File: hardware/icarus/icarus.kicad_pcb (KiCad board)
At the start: 2 copper layers, 0 parts

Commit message: Design with stm32f3
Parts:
- added C1: 1uF, Capacitor_SMD:C_0805_2012Metric, F.Cu at (167.6, 80.0)
- added C10: 10nF, Capacitor_SMD:C_0805_2012Metric, F.Cu at (182.6, 59.7)
- added C11: 100nF, Capacitor_SMD:C_0805_2012Metric, F.Cu at (182.6, 64.3)
- added C2: 1uF, Capacitor_SMD:C_0805_2012Metric, F.Cu at (160.3, 79.5)
- added C3: 4.7uF, Capacitor_SMD:C_0805_2012Metric, F.Cu at (158.0, 58.9)
- added C4: 100nF, Capacitor_SMD:C_0805_2012Metric, F.Cu at (183.9, 77.2)
- added C5: 100nF, Capacitor_SMD:C_0805_2012Metric, F.Cu at (158.0, 68.3)
- added C6: 100nF, Capacitor_SMD:C_0805_2012Metric, F.Cu at (162.1, 57.1)
- added C7: 100nF, Capacitor_SMD:C_0805_2012Metric, F.Cu at (169.2, 68.3)
- added C8: 100nF, Capacitor_SMD:C_0805_2012Metric, F.Cu at (182.6, 62.0)
- added C9: 2.2nF, Capacitor_SMD:C_0805_2012Metric, F.Cu at (174.0, 60.2)
- added D1: PWR, LED_SMD:LED_0805_2012Metric, F.Cu at (164.3, 75.4)
- added D2: STAT1, LED_SMD:LED_0805_2012Metric, F.Cu at (177.3, 54.4)
- added D3: STAT2, LED_SMD:LED_0805_2012Metric, F.Cu at (177.3, 56.6)
- added J1: USB_B_Micro, Connector_USB:USB_Micro-B_Amphenol_10103594-0001LF_Horizontal, F.Cu at (163.8, 86.4)
- added J2: SWJ-DP, Connector_PinHeader_1.27mm:PinHeader_2x05_P1.27mm_Vertical_SMD, F.Cu at (176.8, 71.4)
- added J3: PWR, Connector_PinSocket_2.54mm:PinSocket_1x06_P2.54mm_Vertical, F.Cu at (151.1, 54.6)
- added J4: PWM, Connector_PinSocket_2.54mm:PinSocket_1x06_P2.54mm_Vertical, F.Cu at (178.1, 49.5)
- added J5: COMMS, Connector_PinSocket_2.54mm:PinSocket_1x06_P2.54mm_Vertical, F.Cu at (151.1, 72.4)
- added J6: GPIO, Connector_PinSocket_2.54mm:PinSocket_1x08_P2.54mm_Vertical, F.Cu at (190.8, 61.0)
- added R1: 10k, Resistor_SMD:R_0805_2012Metric, F.Cu at (167.6, 77.7)
- added R2: 100, Resistor_SMD:R_0805_2012Metric, F.Cu at (160.3, 75.4)
- added R3: 10k, Resistor_SMD:R_0805_2012Metric, F.Cu at (156.5, 78.5)
- added R4: 10k, Resistor_SMD:R_0805_2012Metric, F.Cu at (156.5, 80.8)
- added R5: 10k, Resistor_SMD:R_0805_2012Metric, F.Cu at (177.0, 77.2)
- added R6: 100, Resistor_SMD:R_0805_2012Metric, F.Cu at (173.5, 54.4)
- added R7: 100, Resistor_SMD:R_0805_2012Metric, F.Cu at (173.5, 56.6)
- added REF**: mounting_holes_30.5mm, drone:mounting_holes_30.5mm, F.Cu at (171.4, 69.8)
- added SW1: RST, Button_Switch_SMD:SW_Push_1P1T_NO_6x6mm_H9.5mm, F.Cu at (180.1, 83.8)
- added SW2: BOOT, Button_Switch_SMD:SW_Push_1P1T_NO_6x6mm_H9.5mm, F.Cu at (173.2, 83.8)
- added U1: STM32F302C8Tx, Package_QFP:LQFP-48_7x7mm_P0.5mm, F.Cu at (163.6, 63.5)
- added U2: AP2112K-3.3, Package_TO_SOT_SMD:SOT-23-5, F.Cu at (163.6, 79.2)
- added U3: MPU-6050, Sensor_Motion:InvenSense_QFN-24_4x4mm_P0.5mm, F.Cu at (178.1, 62.0)
- added Y1: 12MHz, Crystal:Crystal_SMD_2016-4Pin_2.0x1.6mm, F.Cu at (170.4, 63.8)
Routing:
- net GND: track 0.00 -> 93.0 mm, vias 0 -> 12
- net /sck: track 0.00 -> 61.1 mm, vias 0 -> 2
- net /miso: track 0.00 -> 58.7 mm, vias 0 -> 3
- net +3V3: track 0.00 -> 55.2 mm, vias 0 -> 11
- net VBUS: track 0.00 -> 53.8 mm
- net /sda: track 0.00 -> 53.2 mm, vias 0 -> 2
- net /mosi: track 0.00 -> 52.9 mm, vias 0 -> 1
- net /scl: track 0.00 -> 50.8 mm, vias 0 -> 5
- net /gpio5: track 0.00 -> 44.7 mm, vias 0 -> 2
- net /nreset: track 0.00 -> 43.2 mm, vias 0 -> 2
- net /gpio4: track 0.00 -> 39.1 mm, vias 0 -> 2
- net /gpio1: track 0.00 -> 37.3 mm, vias 0 -> 3
- net /gpio3: track 0.00 -> 36.1 mm, vias 0 -> 2
- net /usb_fs_dm: track 0.00 -> 33.6 mm, vias 0 -> 2
- net /gpio2: track 0.00 -> 33.6 mm, vias 0 -> 1
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- added copper zone on PWR, net +3V3
- added copper zone on B.Cu, net GND
- added copper zone on F.Cu, net GND
- added copper zone on GND, net GND
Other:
- board outline added: 43.7 x 42.4 mm
- copper layers 2 -> 4
- board text added: "1"
- board text added: "2"
- board text added: "3"
- board text added: "3V3"
- board text added: "4"
- board text added: "5"
- board text added: "5V"
- board text added: "6"
- board text added: "G"
- board text added: "RX2"
- board text added: "SCL"
- board text added: "SDA"
- board text added: "TX2"
- board text added: "V"
- board text added: "icarus :: Rev A nnarain"

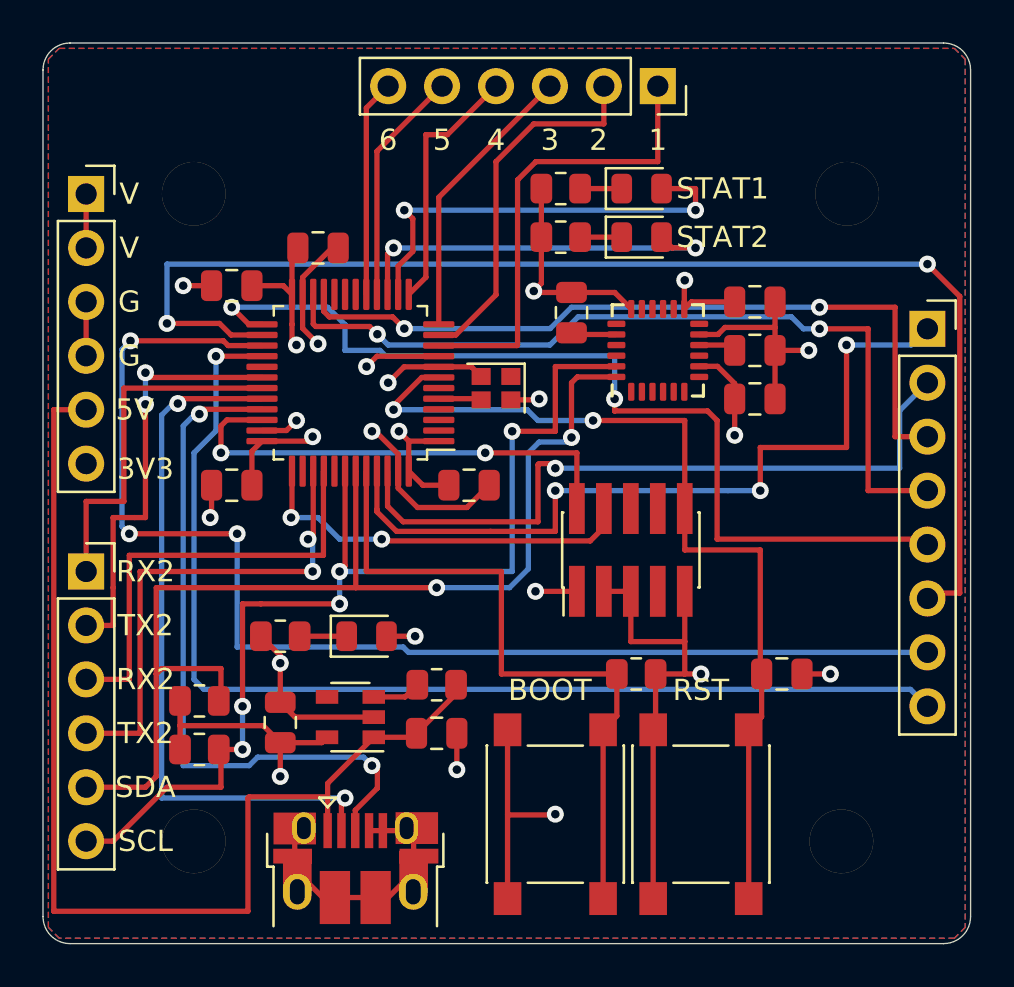
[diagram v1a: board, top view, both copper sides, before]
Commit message: Switch linear regulator
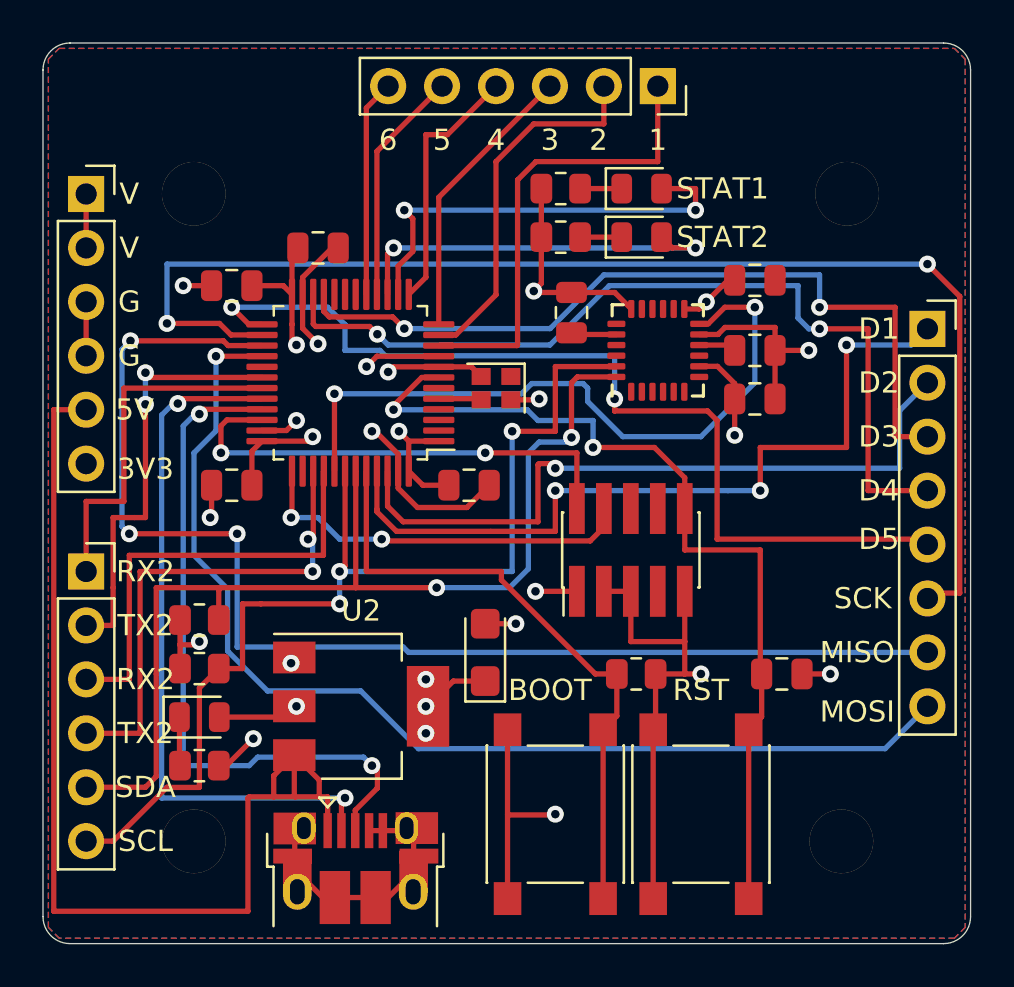
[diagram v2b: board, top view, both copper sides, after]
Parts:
- removed C2: 1uF, Capacitor_SMD:C_0805_2012Metric
- removed R1: 10k, Resistor_SMD:R_0805_2012Metric
- C1: value 1uF -> 22uF; footprint Capacitor_SMD:C_0805_2012Metric -> Capacitor_Tantalum_SMD:CP_EIA-3216-18_Kemet-A
- U2: value AP2112K-3.3 -> AMS1117-3.3; footprint Package_TO_SOT_SMD:SOT-23-5 -> Package_TO_SOT_SMD:SOT-223-3_TabPin2
- moved D1 8.75 mm to (156.5, 79.2)
- moved R2 7.19 mm to (156.5, 81.5), turned to 0 degrees
- moved C1 4.44 mm to (169.9, 76.2), turned to 90 degrees
- moved R3 3.81 mm to (156.5, 74.7)
- moved R4 3.81 mm to (156.5, 77.0)
- moved C10 1.02 mm to (182.6, 58.7)
- moved U2 0.72 mm to (164.1, 78.7), turned to 0 degrees
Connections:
- C1 pad 1: VBUS -> +3V3
- U1 pad 41: Net-(U1-Pad41) -> /imu_int
- U2 pad 1: VBUS -> GND
- U2 pad 2: GND -> +3V3
- U2 pad 3: Net-(R1-Pad2) -> VBUS
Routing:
- net /imu_int: track 0.00 -> 32.6 mm, vias 0 -> 2
- net GND: track 93.0 -> 85.3 mm, vias 12 -> 13
- net +3V3: track 55.2 -> 52.0 mm, vias 11 -> 14
- net /sda: track 53.2 -> 50.1 mm
- net /boot0: track 32.2 -> 29.6 mm
- net Net-(R1-Pad2): track 2.29 -> 0.00 mm
- net /gpio3: track 36.1 -> 38.2 mm
- net /gpio4: track 39.1 -> 41.2 mm
- net VBUS: track 53.8 -> 51.8 mm
- net /nreset: track 43.2 -> 42.3 mm
- net /scl: track 50.8 -> 50.2 mm, vias 5 -> 3
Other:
- board text added: "D1"
- board text added: "D2"
- board text added: "D3"
- board text added: "D4"
- board text added: "D5"
- board text added: "MISO"
- board text added: "MOSI"
- board text added: "SCK"
